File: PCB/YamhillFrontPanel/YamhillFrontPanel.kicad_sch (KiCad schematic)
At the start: 43 parts, among them J1 Conn_01x02, J2 Conn_01x02, J3 4" TFT LCD ST7796S, J4 REF_IN, J5 Speaker, J6 Headphones, SW1 Tune, SW2 Multifunction, U1 Pico, U2 Si5351C, U3 OSCILLATOR, U4 LM4875

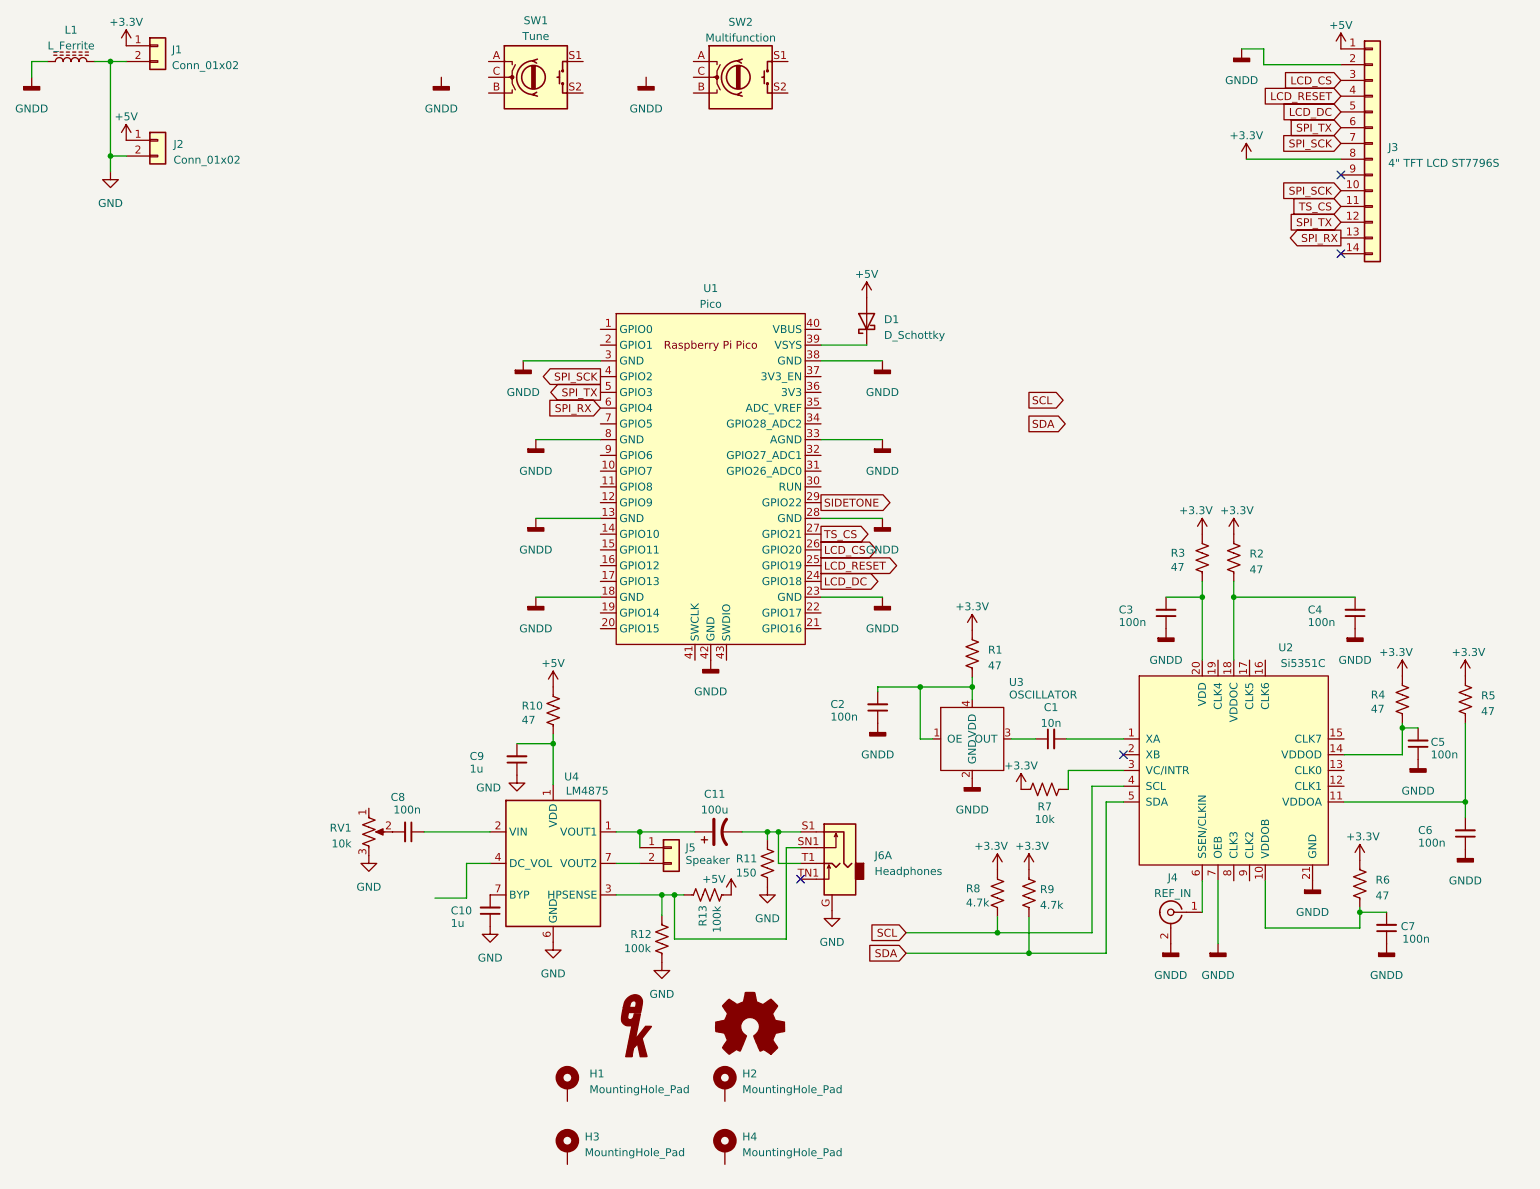
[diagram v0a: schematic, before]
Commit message: First pass of front panel circuit
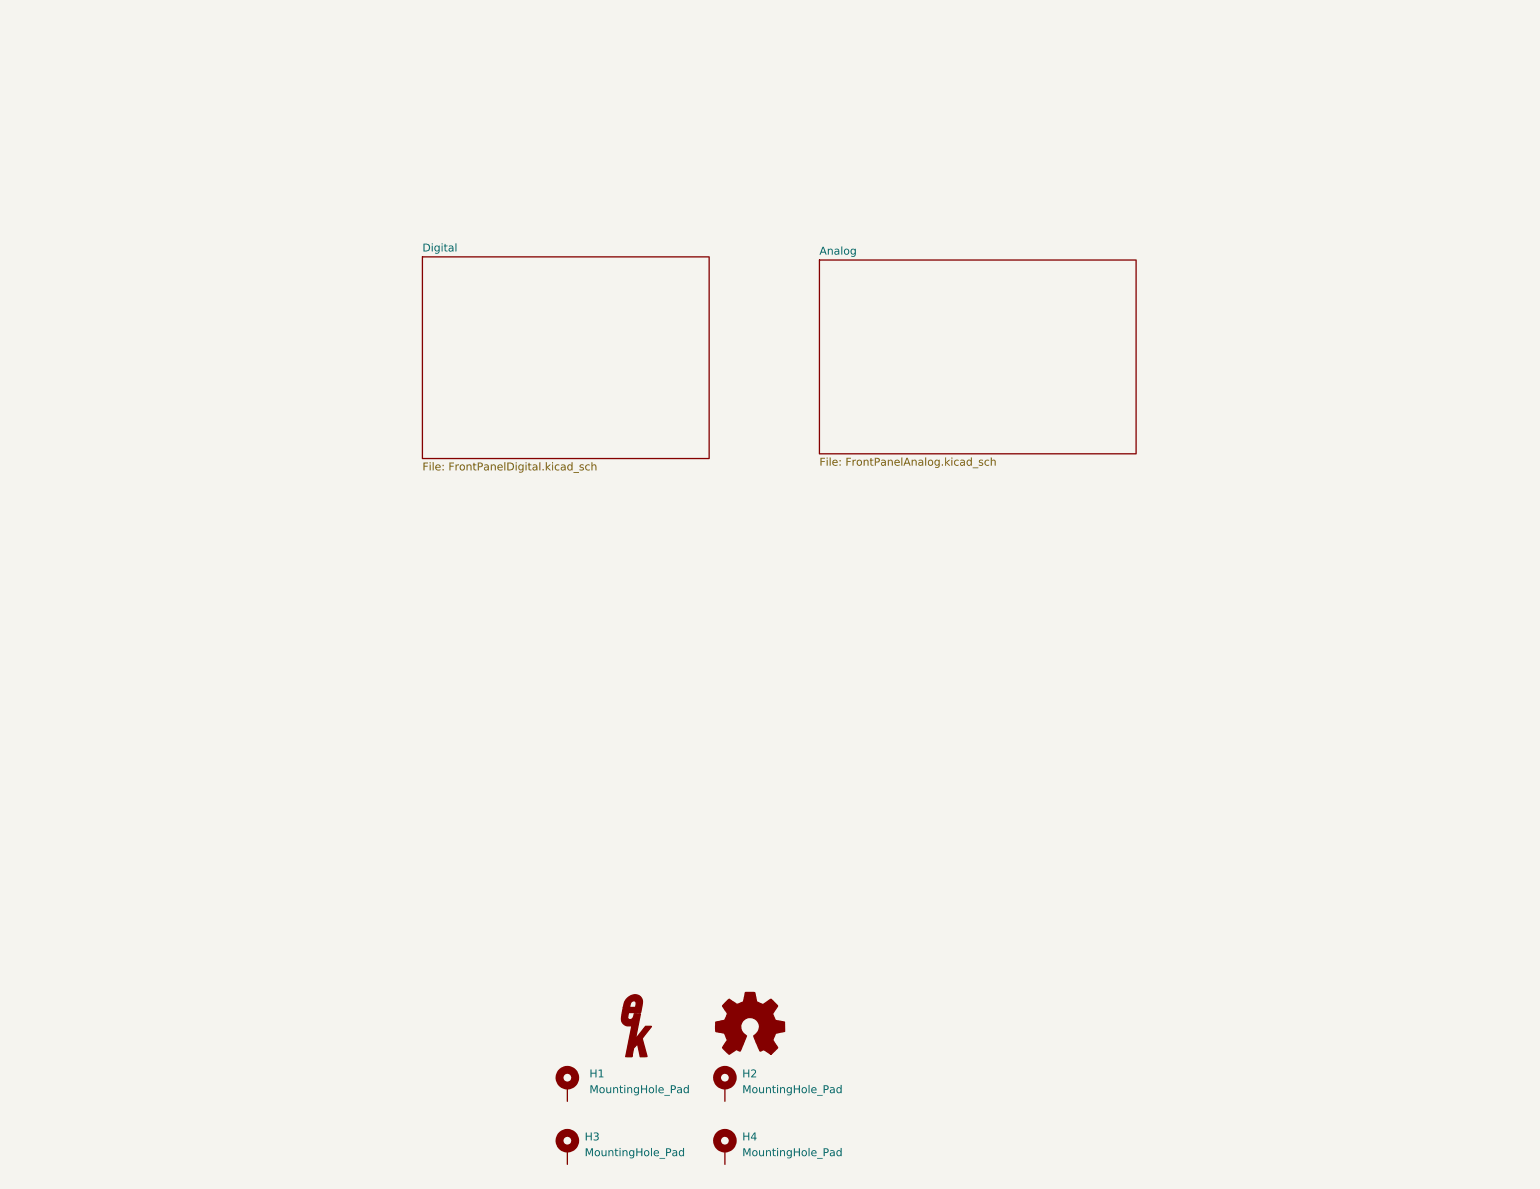
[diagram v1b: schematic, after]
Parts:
- removed C1: 10n, symbol Device:C_Small
- removed C10, C9: 1u, symbol Device:C_Small
- removed C11: 100u, symbol Device:C_Polarized_US
- removed C2, C3, C4, C5, C6, C7, C8: 100n, symbol Device:C_Small
- removed D1: D_Schottky, symbol Device:D_Schottky
- removed J1, J2: Conn_01x02, symbol Connector_Generic:Conn_01x02
- removed J3: 4" TFT LCD ST7796S, symbol Connector_Generic:Conn_01x14
- removed J4: REF_IN, symbol Connector:Conn_Coaxial
- removed J5: Speaker, symbol Connector_Generic:Conn_01x02
- removed J6: Headphones, symbol Connector_Audio:AudioJack2_Dual_Ground_Switch
- removed L1: L_Ferrite, symbol Device:L_Ferrite
- removed R1, R10, R2, R3, R4, R5, R6: 47, symbol Device:R_US
- removed R11: 150, symbol Device:R_US
- removed R12, R13: 100k, symbol Device:R_US
- removed R7: 10k, symbol Device:R_US
- removed R8, R9: 4.7k, symbol Device:R_US
- removed RV1: 10k, symbol Device:R_Potentiometer_US
- removed SW1: Tune, symbol Device:RotaryEncoder_Switch
- removed SW2: Multifunction, symbol Device:RotaryEncoder_Switch
- removed U1: Pico, RPi_Pico:RPi_Pico_SMD_TH, symbol MCU_RaspberryPi_and_Boards:Pico
- removed U2: Si5351C, MODULE, symbol EtherkitKicadLibrary:Si5351BC
- removed U3: OSCILLATOR, symbol EtherkitKicadLibrary:OSCILLATOR
- removed U4: LM4875, Package_SO:TSSOP-8_3x3mm_P0.65mm, symbol EtherkitKicadLibrary:LM4875
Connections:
- no-connect marks 4 -> 0
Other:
- added sheet Analog (FrontPanelAnalog.kicad_sch)
- added sheet Digital (FrontPanelDigital.kicad_sch)

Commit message: Rev A Front Panel
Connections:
- net GNDD: now reaches H3.1
- net GNDD: now also H1.1, H2.1, H4.1
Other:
- moved on the sheet: H1, H2, H3, H4
